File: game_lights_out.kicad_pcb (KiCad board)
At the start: 2 copper layers, 171.2 x 136.9 mm, 94 parts, among them SW1 SW_MEC_5E, SW10 SW_MEC_5E, SW11 SW_MEC_5E, SW12 SW_MEC_5E, SW13 SW_MEC_5E, SW14 SW_MEC_5E, SW15 SW_MEC_5E, SW16 SW_MEC_5E, SW17 SW_MEC_5E, SW18 SW_MEC_5E, SW19 SW_MEC_5E, SW2 SW_MEC_5E, SW20 SW_MEC_5E, SW21 SW_MEC_5E, SW22 SW_MEC_5E, SW23 SW_MEC_5E, SW24 SW_MEC_5E, SW25 SW_MEC_5E, SW26 SW_MEC_5E, SW27 SW_MEC_5E, SW28 SW_MEC_5E, SW29 SW_MEC_5E, SW3 SW_MEC_5E, SW30 SW_MEC_5E, SW31 SW_MEC_5E, SW32 SW_MEC_5E, SW33 SW_MEC_5E, SW34 SW_MEC_5E, SW35 SW_MEC_5E, SW36 SW_MEC_5E, SW37 SW_MEC_5E, SW38 SW_MEC_5E, SW39 SW_MEC_5E, SW4 SW_MEC_5E, SW40 SW_MEC_5E, SW5 SW_MEC_5E, SW6 SW_MEC_5E, SW7 SW_MEC_5E, SW8 SW_MEC_5E, SW9 SW_MEC_5E, U1 ATmega328-P, U2 ULN2803A

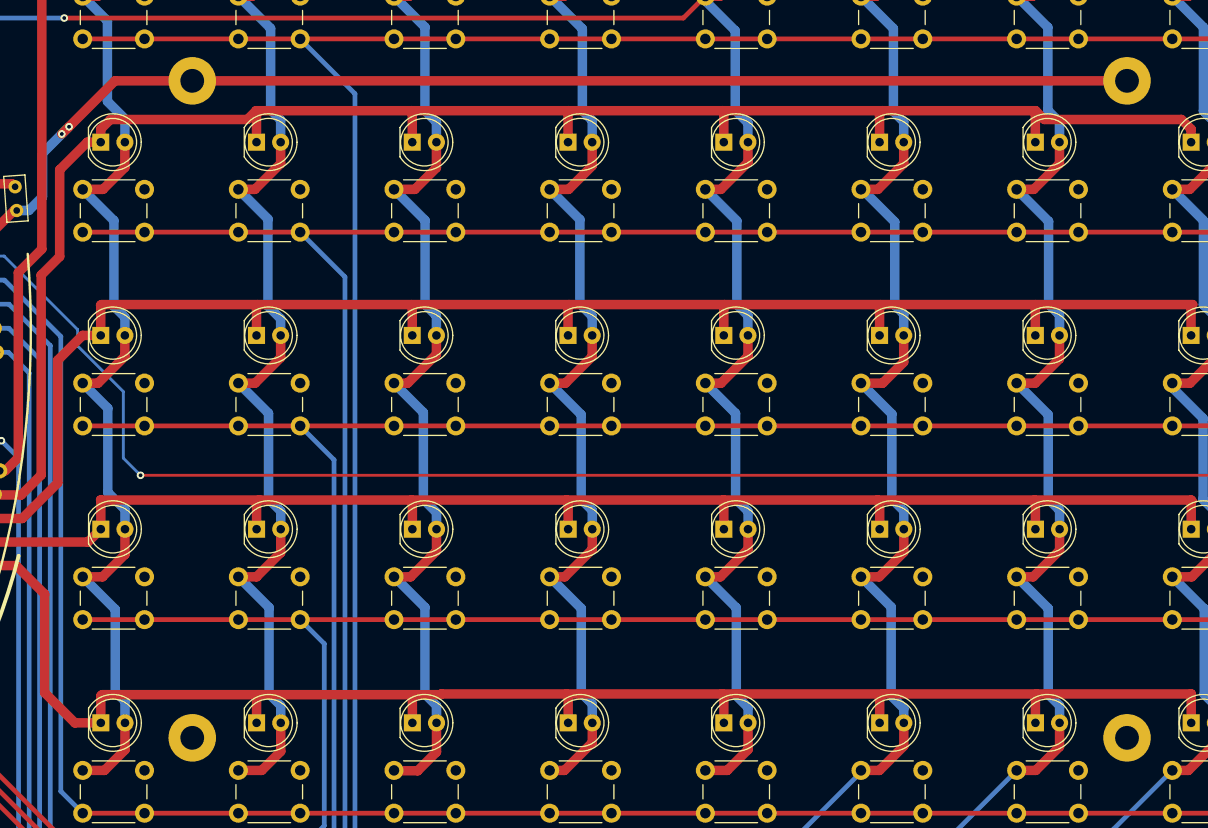
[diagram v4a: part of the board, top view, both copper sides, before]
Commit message: Fixed placement of holes and size of power vias
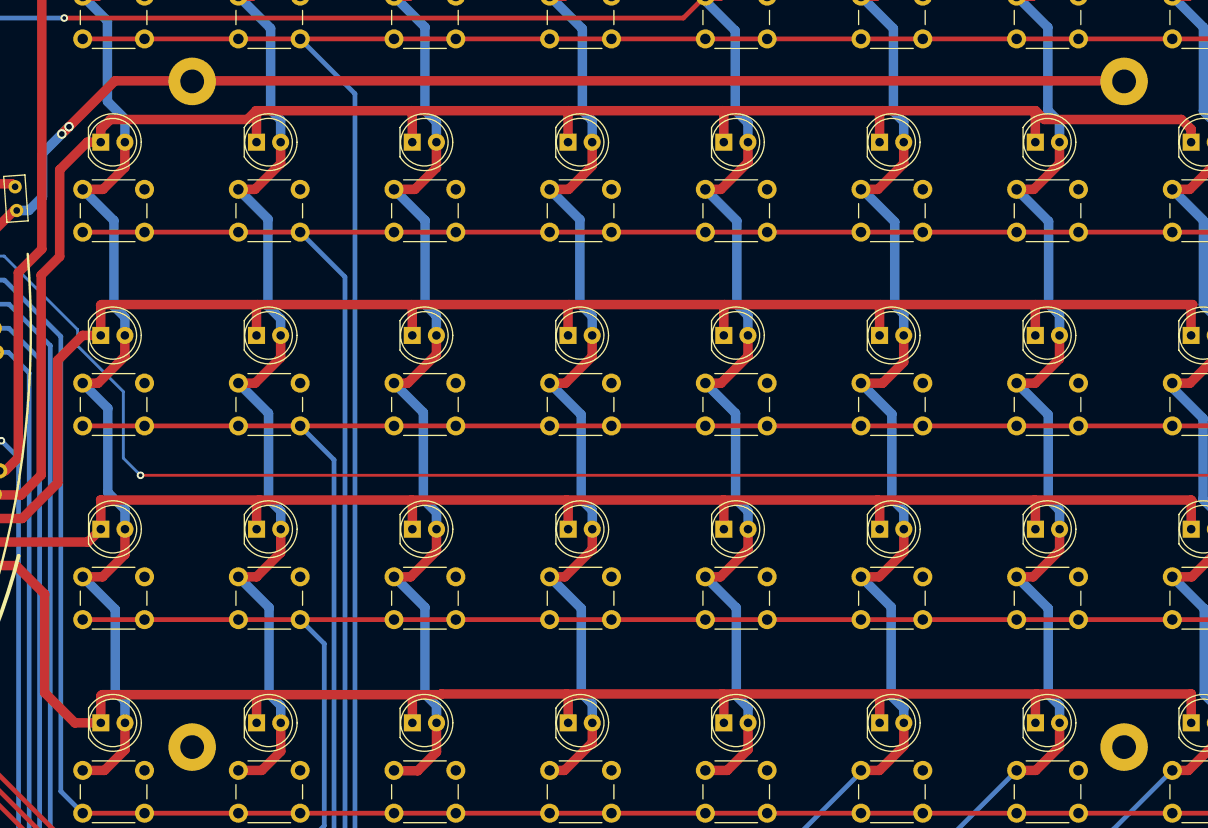
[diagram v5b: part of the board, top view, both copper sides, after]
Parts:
- moved H2 1.02 mm to (162.0, 145.5)
- moved H1 0.97 mm to (64.0, 145.5)
- moved H4 0.31 mm to (162.0, 75.5)
- moved H3 0.06 mm to (64.0, 75.5)
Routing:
- net RST: track 227.2 -> 225.0 mm
